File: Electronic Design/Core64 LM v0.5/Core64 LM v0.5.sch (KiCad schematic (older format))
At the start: 67 parts, among them J1 Digi-Key 77311-420-36LF-ND, J2 Digi-Key 77311-420-36LF-ND

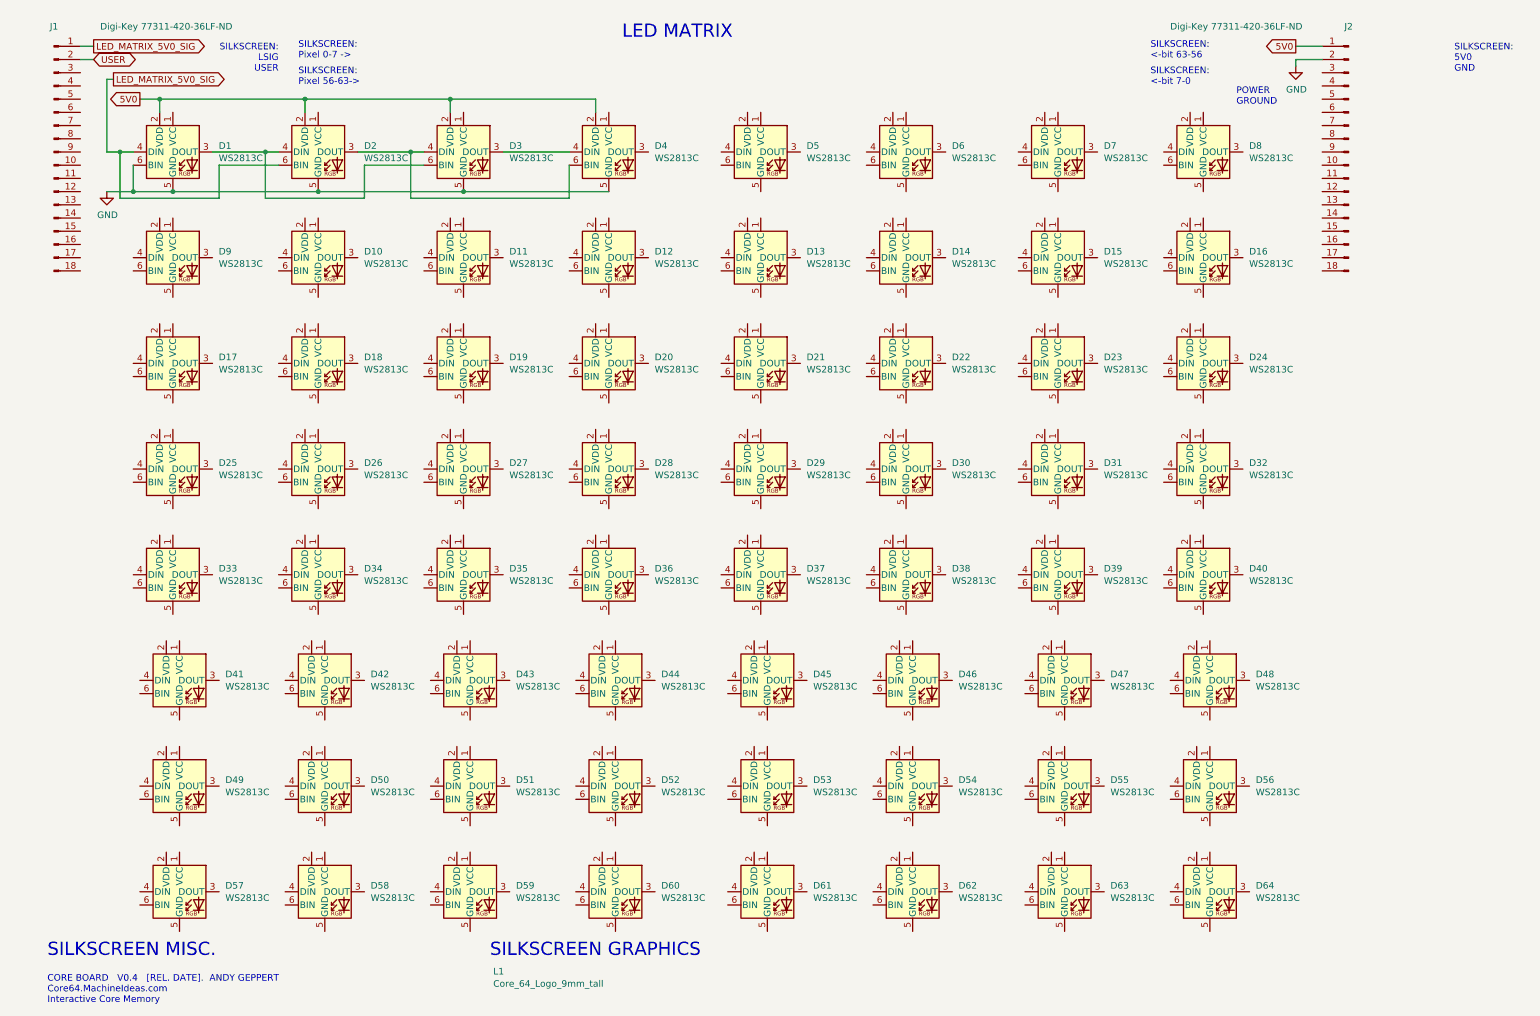
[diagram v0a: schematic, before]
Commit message: Layout LED Matrix and add WS2812/13 data sheets
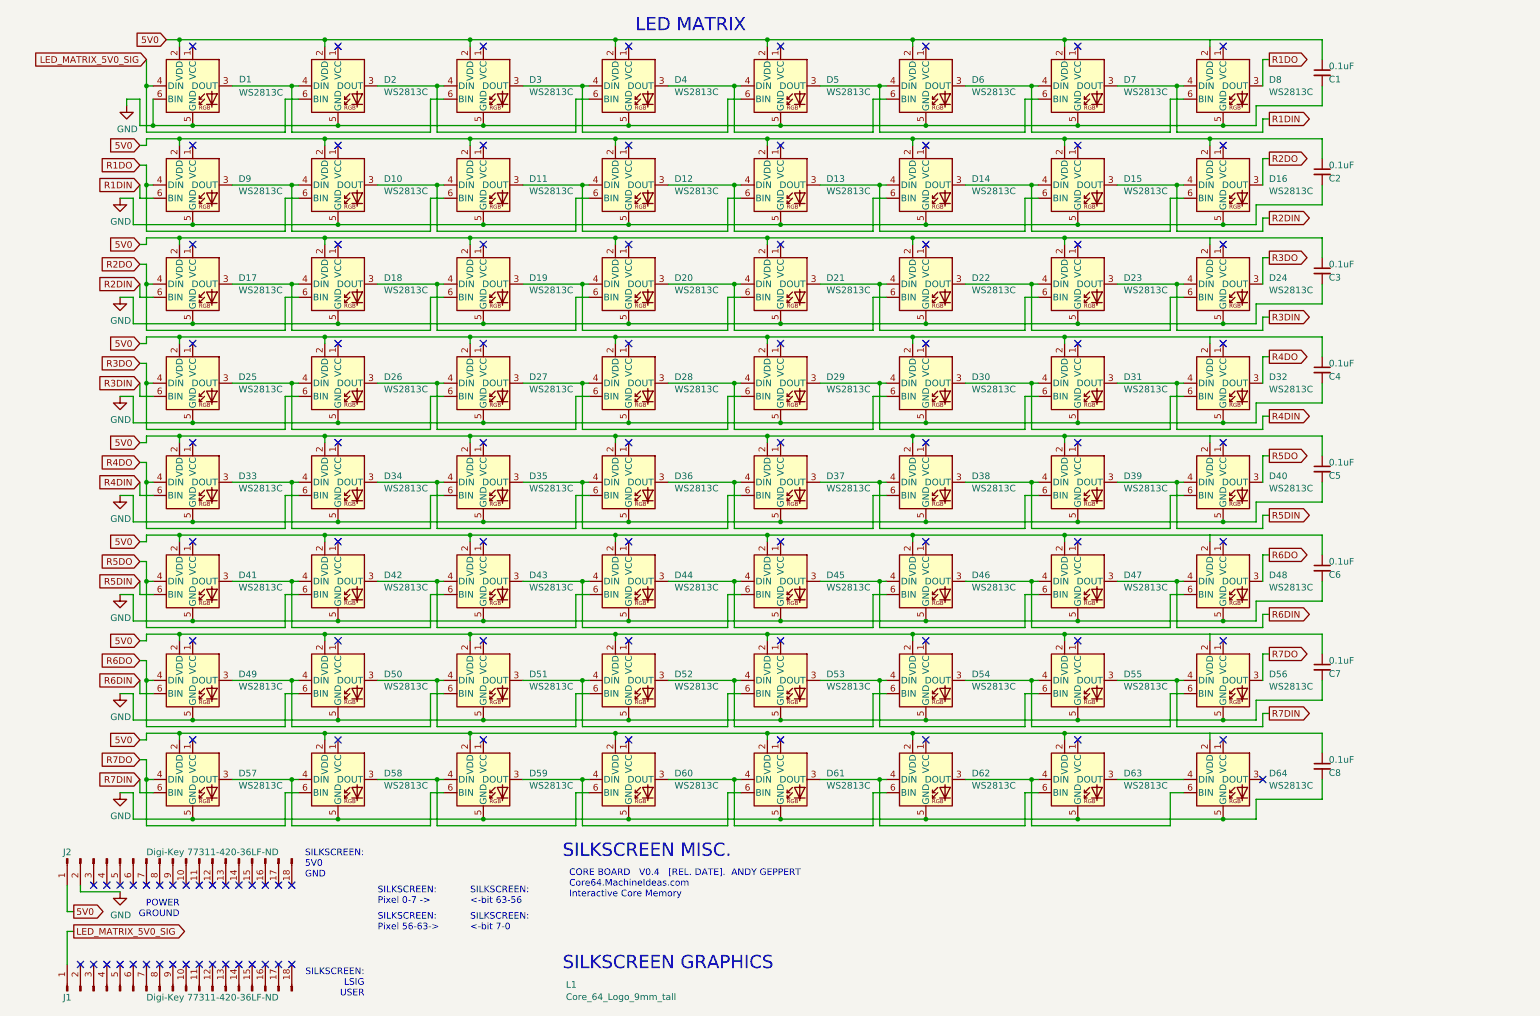
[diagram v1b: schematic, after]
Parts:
- added C1, C2, C3, C4, C5, C6, C7, C8: 0.1uF, Capacitor_SMD:C_0603_1608Metric, symbol Device:C_Small
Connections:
- net 5V0: now also D10.2 (VDD), D11.2 (VDD), D12.2 (VDD), D13.2 (VDD), D14.2 (VDD), D15.2 (VDD), D16.2 (VDD), D17.2 (VDD), D18.2 (VDD), D19.2 (VDD), D20.2 (VDD), D21.2 (VDD), D22.2 (VDD), D23.2 (VDD), D24.2 (VDD), D25.2 (VDD), D26.2 (VDD), D27.2 (VDD), D28.2 (VDD), D29.2 (VDD), D30.2 (VDD), D31.2 (VDD), D32.2 (VDD), D33.2 (VDD), D34.2 (VDD), D35.2 (VDD), D36.2 (VDD), D37.2 (VDD), D38.2 (VDD), D39.2 (VDD), D40.2 (VDD), D41.2 (VDD), D42.2 (VDD), D43.2 (VDD), D44.2 (VDD), D45.2 (VDD), D46.2 (VDD), D47.2 (VDD), D48.2 (VDD), D49.2 (VDD), D5.2 (VDD), D50.2 (VDD), D51.2 (VDD), D52.2 (VDD), D53.2 (VDD), D54.2 (VDD), D55.2 (VDD), D56.2 (VDD), D57.2 (VDD), D58.2 (VDD), D59.2 (VDD), D6.2 (VDD), D60.2 (VDD), D61.2 (VDD), D62.2 (VDD), D63.2 (VDD), D64.2 (VDD), D7.2 (VDD), D8.2 (VDD), D9.2 (VDD), C1.1, C2.1, C3.1, C4.1, C5.1, C6.1, C7.1, C8.1
- net GND: now also D10.5 (GND), D11.5 (GND), D12.5 (GND), D13.5 (GND), D14.5 (GND), D15.5 (GND), D16.5 (GND), D17.5 (GND), D18.5 (GND), D19.5 (GND), D20.5 (GND), D21.5 (GND), D22.5 (GND), D23.5 (GND), D24.5 (GND), D25.5 (GND), D26.5 (GND), D27.5 (GND), D28.5 (GND), D29.5 (GND), D30.5 (GND), D31.5 (GND), D32.5 (GND), D33.5 (GND), D34.5 (GND), D35.5 (GND), D36.5 (GND), D37.5 (GND), D38.5 (GND), D39.5 (GND), D40.5 (GND), D41.5 (GND), D42.5 (GND), D43.5 (GND), D44.5 (GND), D45.5 (GND), D46.5 (GND), D47.5 (GND), D48.5 (GND), D49.5 (GND), D5.5 (GND), D50.5 (GND), D51.5 (GND), D52.5 (GND), D53.5 (GND), D54.5 (GND), D55.5 (GND), D56.5 (GND), D57.5 (GND), D58.5 (GND), D59.5 (GND), D6.5 (GND), D60.5 (GND), D61.5 (GND), D62.5 (GND), D63.5 (GND), D64.5 (GND), D7.5 (GND), D8.5 (GND), D9.5 (GND), C1.2, C2.2, C3.2, C4.2, C5.2, C6.2, C7.2, C8.2
- net at D3.3 (DOUT), D4.4 (DIN): now also D5.6 (BIN)
- net at D4.3 (DOUT): now also D5.4 (DIN), D6.6 (BIN)
- net at D5.3 (DOUT): now also D6.4 (DIN), D7.6 (BIN)
- net at D6.3 (DOUT): now also D7.4 (DIN), D8.6 (BIN)
- net R1DIN: now reaches D7.3 (DOUT)
- net R1DIN: now also D8.4 (DIN), D9.6 (BIN)
- net R1DO: now reaches D8.3 (DOUT)
- net R1DO: now also D10.6 (BIN), D9.4 (DIN)
- net at D9.3 (DOUT): now also D10.4 (DIN), D11.6 (BIN)
- net at D11.3 (DOUT): now also D12.4 (DIN), D13.6 (BIN)
- net at D11.4 (DIN): now also D10.3 (DOUT), D12.6 (BIN)
- net at D12.3 (DOUT): now also D13.4 (DIN), D14.6 (BIN)
- net at D13.3 (DOUT): now also D14.4 (DIN), D15.6 (BIN)
- net at D14.3 (DOUT): now also D15.4 (DIN), D16.6 (BIN)
- net R2DIN: now reaches D15.3 (DOUT)
- net R2DIN: now also D16.4 (DIN), D17.6 (BIN)
- net R2DO: now reaches D16.3 (DOUT)
- net R2DO: now also D17.4 (DIN), D18.6 (BIN)
- net at D17.3 (DOUT): now also D18.4 (DIN), D19.6 (BIN)
- net at D19.3 (DOUT): now also D20.4 (DIN), D21.6 (BIN)
- net at D19.4 (DIN): now also D18.3 (DOUT), D20.6 (BIN)
- net at D20.3 (DOUT): now also D21.4 (DIN), D22.6 (BIN)
- net at D21.3 (DOUT): now also D22.4 (DIN), D23.6 (BIN)
- net at D22.3 (DOUT): now also D23.4 (DIN), D24.6 (BIN)
- net R3DIN: now reaches D23.3 (DOUT)
- net R3DIN: now also D24.4 (DIN), D25.6 (BIN)
- net R3DO: now reaches D24.3 (DOUT)
- net R3DO: now also D25.4 (DIN), D26.6 (BIN)
- net at D25.3 (DOUT): now also D26.4 (DIN), D27.6 (BIN)
- net at D27.3 (DOUT): now also D28.4 (DIN), D29.6 (BIN)
- net at D27.4 (DIN): now also D26.3 (DOUT), D28.6 (BIN)
- net at D28.3 (DOUT): now also D29.4 (DIN), D30.6 (BIN)
- net at D29.3 (DOUT): now also D30.4 (DIN), D31.6 (BIN)
- net at D30.3 (DOUT): now also D31.4 (DIN), D32.6 (BIN)
- net R4DIN: now reaches D31.3 (DOUT)
- net R4DIN: now also D32.4 (DIN), D33.6 (BIN)
- net R4DO: now reaches D32.3 (DOUT)
- net R4DO: now also D33.4 (DIN), D34.6 (BIN)
- net at D33.3 (DOUT): now also D34.4 (DIN), D35.6 (BIN)
- net at D35.3 (DOUT): now also D36.4 (DIN), D37.6 (BIN)
- net at D35.4 (DIN): now also D34.3 (DOUT), D36.6 (BIN)
- net at D36.3 (DOUT): now also D37.4 (DIN), D38.6 (BIN)
- net at D37.3 (DOUT): now also D38.4 (DIN), D39.6 (BIN)
- net at D38.3 (DOUT): now also D39.4 (DIN), D40.6 (BIN)
- net R5DIN: now reaches D39.3 (DOUT)
- net R5DIN: now also D40.4 (DIN), D41.6 (BIN)
- net R5DO: now reaches D40.3 (DOUT)
- net R5DO: now also D41.4 (DIN), D42.6 (BIN)
- net at D41.3 (DOUT): now also D42.4 (DIN), D43.6 (BIN)
- net at D43.3 (DOUT): now also D44.4 (DIN), D45.6 (BIN)
- net at D43.4 (DIN): now also D42.3 (DOUT), D44.6 (BIN)
- net at D44.3 (DOUT): now also D45.4 (DIN), D46.6 (BIN)
- net at D45.3 (DOUT): now also D46.4 (DIN), D47.6 (BIN)
- net at D46.3 (DOUT): now also D47.4 (DIN), D48.6 (BIN)
- net R6DIN: now reaches D47.3 (DOUT)
- net R6DIN: now also D48.4 (DIN), D49.6 (BIN)
- net R6DO: now reaches D48.3 (DOUT)
- net R6DO: now also D49.4 (DIN), D50.6 (BIN)
- net at D49.3 (DOUT): now also D50.4 (DIN), D51.6 (BIN)
- net at D51.3 (DOUT): now also D52.4 (DIN), D53.6 (BIN)
- net at D51.4 (DIN): now also D50.3 (DOUT), D52.6 (BIN)
- net at D52.3 (DOUT): now also D53.4 (DIN), D54.6 (BIN)
- net at D53.3 (DOUT): now also D54.4 (DIN), D55.6 (BIN)
- net at D54.3 (DOUT): now also D55.4 (DIN), D56.6 (BIN)
- net R7DIN: now reaches D55.3 (DOUT)
- net R7DIN: now also D56.4 (DIN), D57.6 (BIN)
- net R7DO: now reaches D56.3 (DOUT)
- net R7DO: now also D57.4 (DIN), D58.6 (BIN)
- net at D57.3 (DOUT): now also D58.4 (DIN), D59.6 (BIN)
- net at D59.3 (DOUT): now also D60.4 (DIN), D61.6 (BIN)
- net at D59.4 (DIN): now also D58.3 (DOUT), D60.6 (BIN)
- net at D60.3 (DOUT): now also D61.4 (DIN), D62.6 (BIN)
- net at D61.3 (DOUT): now also D62.4 (DIN), D63.6 (BIN)
- net at D62.3 (DOUT): now also D63.4 (DIN), D64.6 (BIN)
- net at D63.3 (DOUT): now also D64.4 (DIN)
- net USER: no longer names the net of J1.2 (Pin_2)
- no-connect marks 0 -> 98
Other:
- moved on the sheet: D1, D10, D11, D12, D13, D14, D15, D16, D2, D3, D4, D5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

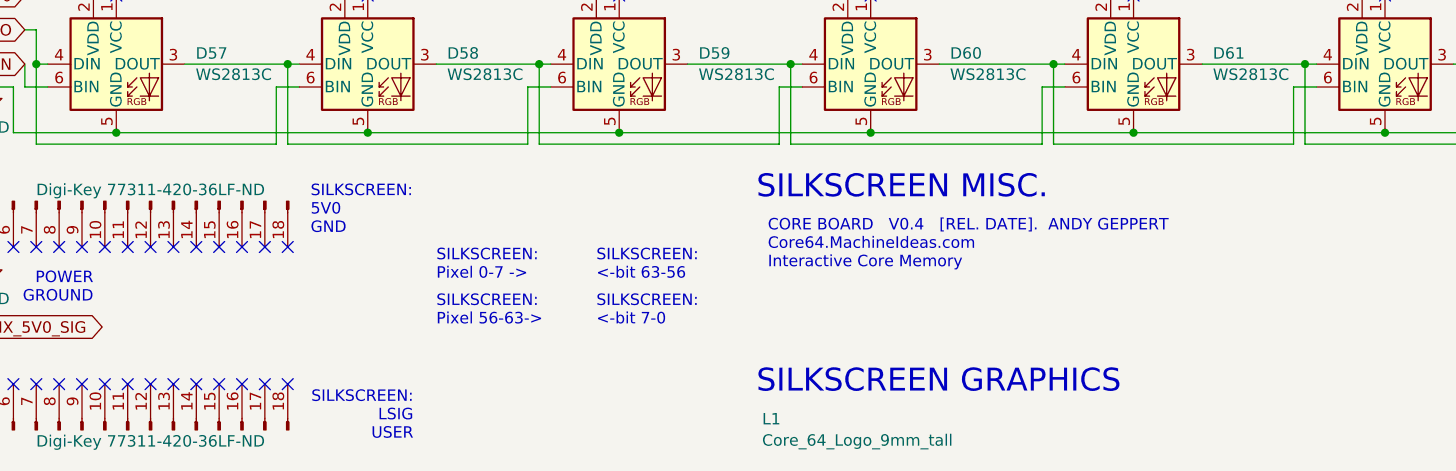
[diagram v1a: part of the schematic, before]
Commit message: Completed LED Matrix layout
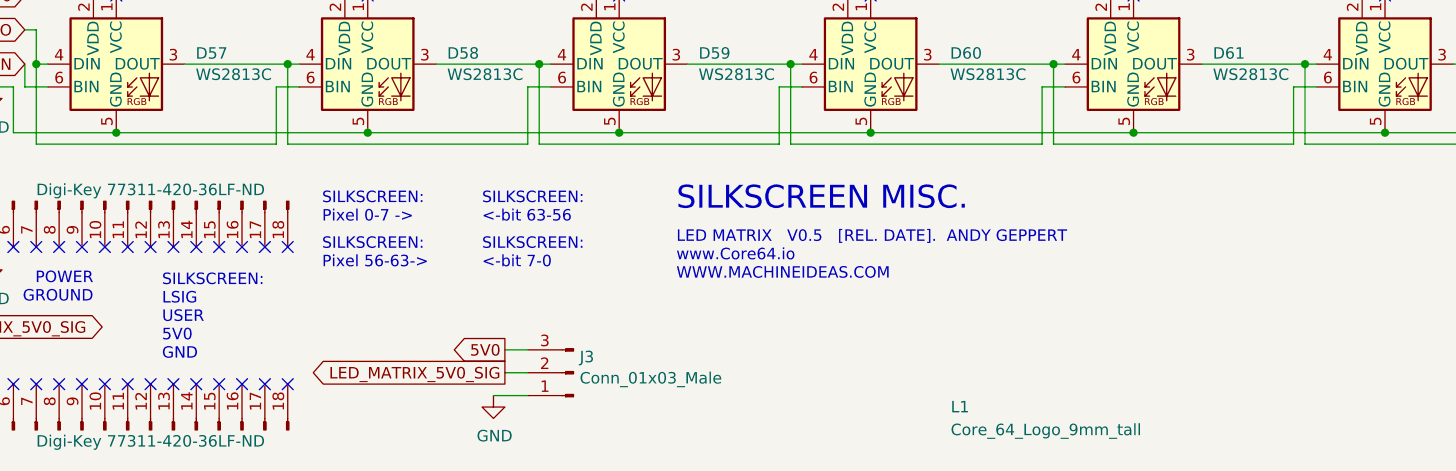
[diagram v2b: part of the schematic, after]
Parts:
- added J3: Conn_01x03_Male, Connector_PinHeader_2.54mm:PinHeader_1x03_P2.54mm_Vertical, symbol Connector:Conn_01x03_Male
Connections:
- net 5V0: now also J3.3 (Pin_3)
- net GND: now also J3.1 (Pin_1)
- net LED_MATRIX_5V0_SIG: now also J3.2 (Pin_2)
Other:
- note added: "LED MATRIX V0.5 [REL. DATE]. ANDY GEPPERT \nwww.Core64.io\nWWW.MACHINEIDEAS.COM"
- note added: "SILKSCREEN:\nLSIG\nUSER\n5V0\nGND"
- note removed: "CORE BOARD V0.4 [REL. DATE]. ANDY GEPPERT \nCore64.MachineIdeas.com\nInteractive Core Memory"
- note removed: "SILKSCREEN GRAPHICS"
- note removed: "SILKSCREEN:\n5V0\nGND"
- note removed: "SILKSCREEN:\nLSIG\nUSER"
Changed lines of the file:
@@
 Text GLabel 750  7450 2    50   Output ~ 0
 LED_MATRIX_5V0_SIG
-Text Notes 2950 7950 2    50   ~ 0
-SILKSCREEN:\nLSIG\nUSER
+Text Notes 1850 7600 0    50   ~ 0
+SILKSCREEN:\nLSIG\nUSER\n5V0\nGND
 $Comp
 L Connector:Conn_01x18_Male J2
@@
 	0    -1   1    0
 $EndComp
-Text Notes 2500 7050 0    50   ~ 0
-SILKSCREEN:\n5V0\nGND
 Text Notes 1550 7350 2    50   ~ 0
 POWER\nGROUND
-Text Notes 4450 7750 0    100  ~ 0
-SILKSCREEN GRAPHICS
 Text Notes 5000 650  0    100  ~ 0
 LED MATRIX
-Text Notes 3050 7250 0    50   ~ 0
+Text Notes 2550 7000 0    50   ~ 0
 SILKSCREEN:\nPixel 0-7 ->
-Text Notes 3750 7250 0    50   ~ 0
+Text Notes 3250 7000 0    50   ~ 0
 SILKSCREEN:\n<-bit 63-56
-Text Notes 3750 7450 0    50   ~ 0
+Text Notes 3250 7200 0    50   ~ 0
 SILKSCREEN:\n<-bit 7-0
-Text Notes 3050 7450 0    50   ~ 0
+Text Notes 2550 7200 0    50   ~ 0
 SILKSCREEN:\nPixel 56-63->
-Text Notes 4500 7200 0    50   ~ 0
-CORE BOARD   V0.4   [REL. DATE].  ANDY GEPPERT   \nCore64.MachineIdeas.com\nInteractive Core Memory
-Text Notes 4450 6900 0    100  ~ 0
+Text Notes 4100 7250 0    50   ~ 0
+LED MATRIX   V0.5   [REL. DATE].  ANDY GEPPERT   \nwww.Core64.io\nWWW.MACHINEIDEAS.COM
+Text Notes 4100 6950 0    100  ~ 0
 SILKSCREEN MISC.
 $Comp
 L CORE_64_LIBRARY:Core_64_Logo_9mm_tall L1
 U 1 1 5F3DC9AF
-P 4450 7900
-F 0 "L1" H 4475 7947 50  0000 L CNN
-F 1 "Core_64_Logo_9mm_tall" H 4475 7854 50  0000 L CNN
-F 2 "Core_Memory_8x8_Array:Core64_Logo_9mm_tall" H 4450 7900 50  0001 C CNN
-F 3 "" H 4450 7900 50  0001 C CNN
-	1    4450 7900
+P 5250 7850
+F 0 "L1" H 5300 7900 50  0000 L CNN
+F 1 "Core_64_Logo_9mm_tall" H 5300 7800 50  0000 L CNN
+F 2 "Core_Memory_8x8_Array:Core64_Logo_9mm_tall" H 5250 7850 50  0001 C CNN
+F 3 "" H 5250 7850 50  0001 C CNN
+	1    5250 7850
 	1    0    0    -1
 $EndComp
@@
 Connection ~ 2750 2850
 Connection ~ 1650 2850
+$Comp
+L Connector:Conn_01x03_Male J3
+U 1 1 606660CA
+P 3650 7650
+F 0 "J3" H 3623 7581 50  0000 R CNN
+F 1 "Conn_01x03_Male" H 3623 7674 50  0000 R CNN
+F 2 "Connector_PinHeader_2.54mm:PinHeader_1x03_P2.54mm_Vertical" H 3650 7650 50  0001 C CNN
+F 3 "~" H 3650 7650 50  0001 C CNN
+	1    3650 7650
+	-1   0    0    1
+$EndComp
+$Comp
+L power:GND #PWR0110
+U 1 1 606661A7
+P 3300 7750
+F 0 "#PWR0110" H 3300 7500 50  0001 C CNN
+F 1 "GND" H 3305 7573 50  0000 C CNN
+F 2 "" H 3300 7750 50  0001 C CNN
+F 3 "" H 3300 7750 50  0001 C CNN
+	1    3300 7750
+	1    0    0    -1
+$EndComp
+Text GLabel 3350 7650 0    50   Output ~ 0
+LED_MATRIX_5V0_SIG
+Text GLabel 3350 7550 0    50   Output ~ 0
+5V0
+Wire Wire Line
+	3350 7550 3450 7550
+Wire Wire Line
+	3350 7650 3450 7650
+Wire Wire Line
+	3300 7750 3450 7750
 $EndSCHEMATC

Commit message: Refine LED Matrix board silk screen details
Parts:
- D1, D10, D11, D12, D13, D14, D15, D16, D17, D18, D19, D2, D20, D21, D22, D23, D24, D25, D26, D27, D28, D29, D3, D30, D31, D32, D33, D34, D35, D36, D37, D38, D39, D4, D40, D41, D42, D43, D44, D45, D46, D47, D48, D49, D5, D50, D51, D52, D53, D54, D55, D56, D57, D58, D59, D6, D60, D61, D62, D63, D64, D7, D8, D9: value WS2813C -> WS2813
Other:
- note added: "CORE64 LED MATRIX (LM) V0.5 [DESIGN RELEASE DATE]\nProject information at www.Core64.io\nDesigned by Andy Geppert at www.MachineIdeas.com\nWS2813 LEDs"
- note added: "SILKSCREEN F/B:\n5V0, LSIG, GND"
- note added: "SILKSCREEN F/B:\nLSIG, USER\n5V0, GND"
- note removed: "LED MATRIX V0.5 [REL. DATE]. ANDY GEPPERT \nwww.Core64.io\nWWW.MACHINEIDEAS.COM"
- note removed: "SILKSCREEN:\nLSIG\nUSER\n5V0\nGND"
